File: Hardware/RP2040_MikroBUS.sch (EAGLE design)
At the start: 78 parts, among them J1 SWD, J3 Qwiic, J5 USB C, J6 microSD, J9 MIKROBUS_SMD_BLACK1, Q1 20V/4.2A/52mΩ/1.4W, U2 MAX17048, U3 MCP73831, U4 W25QXX128MBIT, U5 RP2040, U7 3.3V, Y2 12MHz

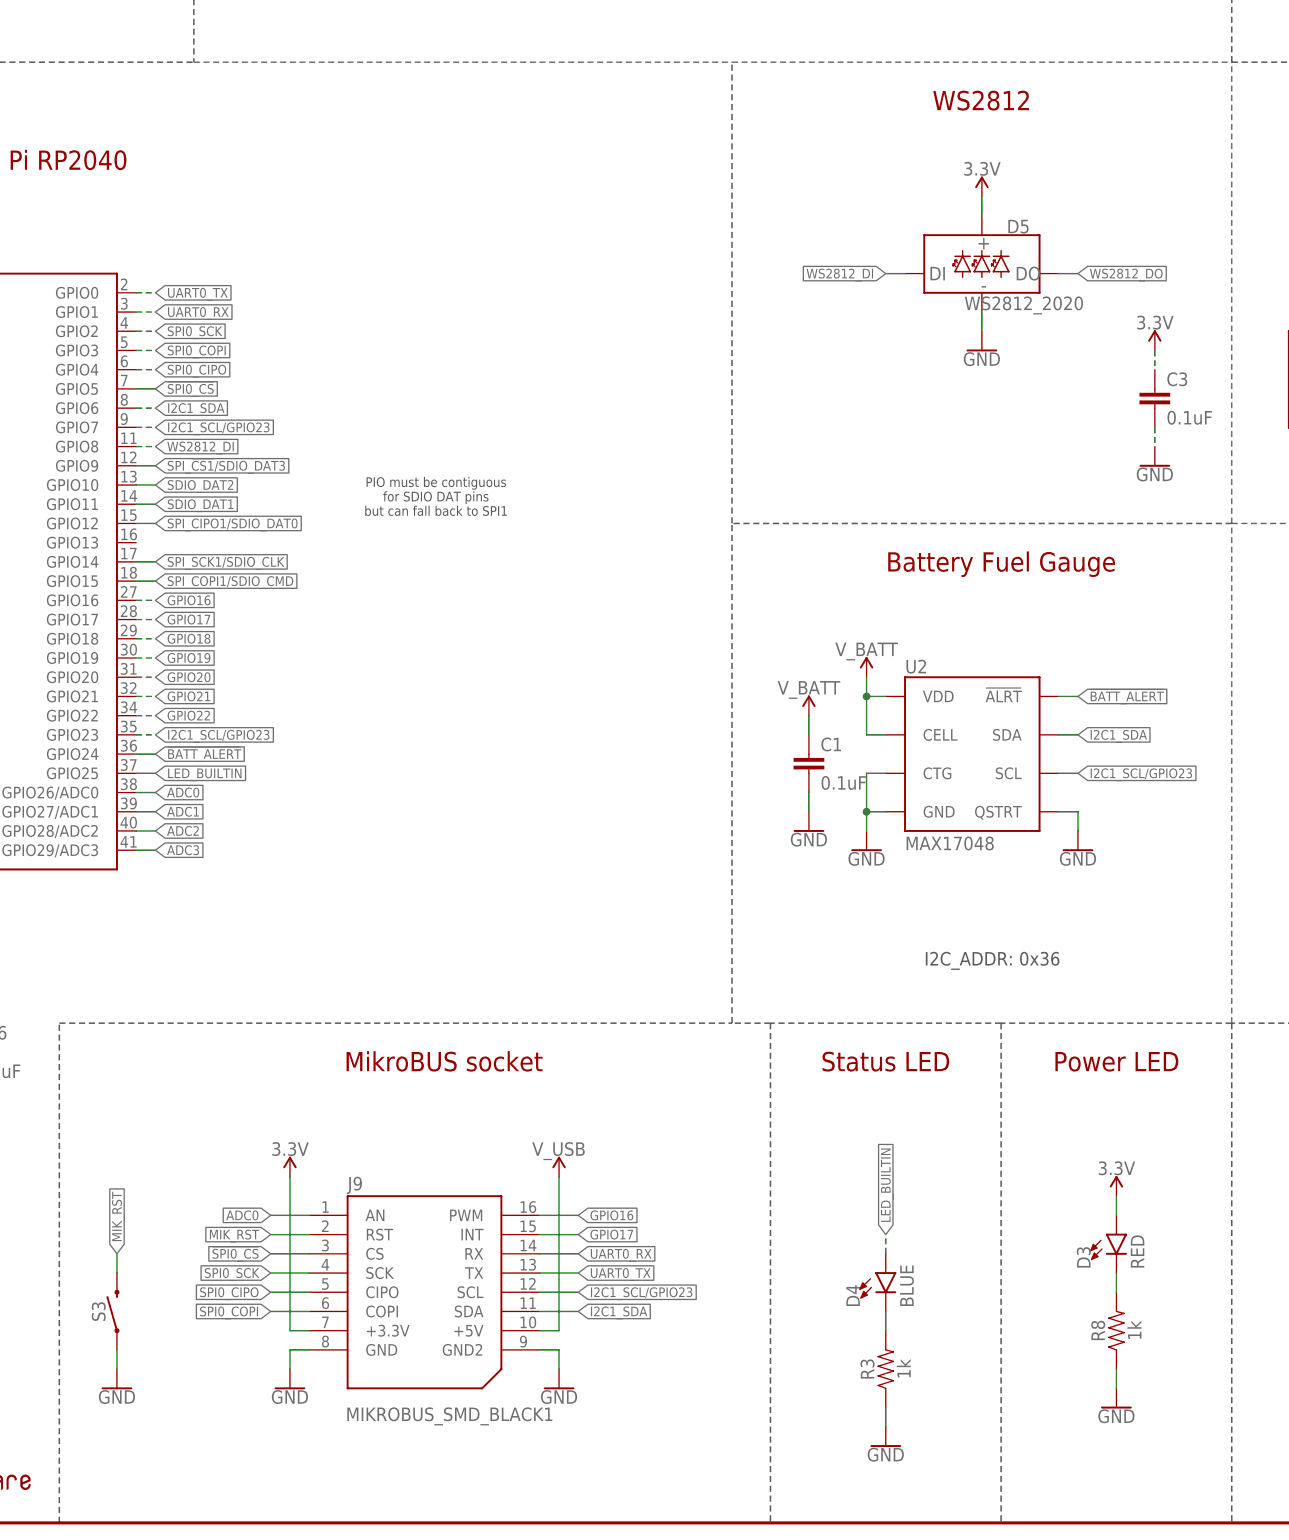
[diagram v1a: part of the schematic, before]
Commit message: Design review before ordering changes
* Add a pullup and NC jumper on the CS line
* A jumper on the PWR LED
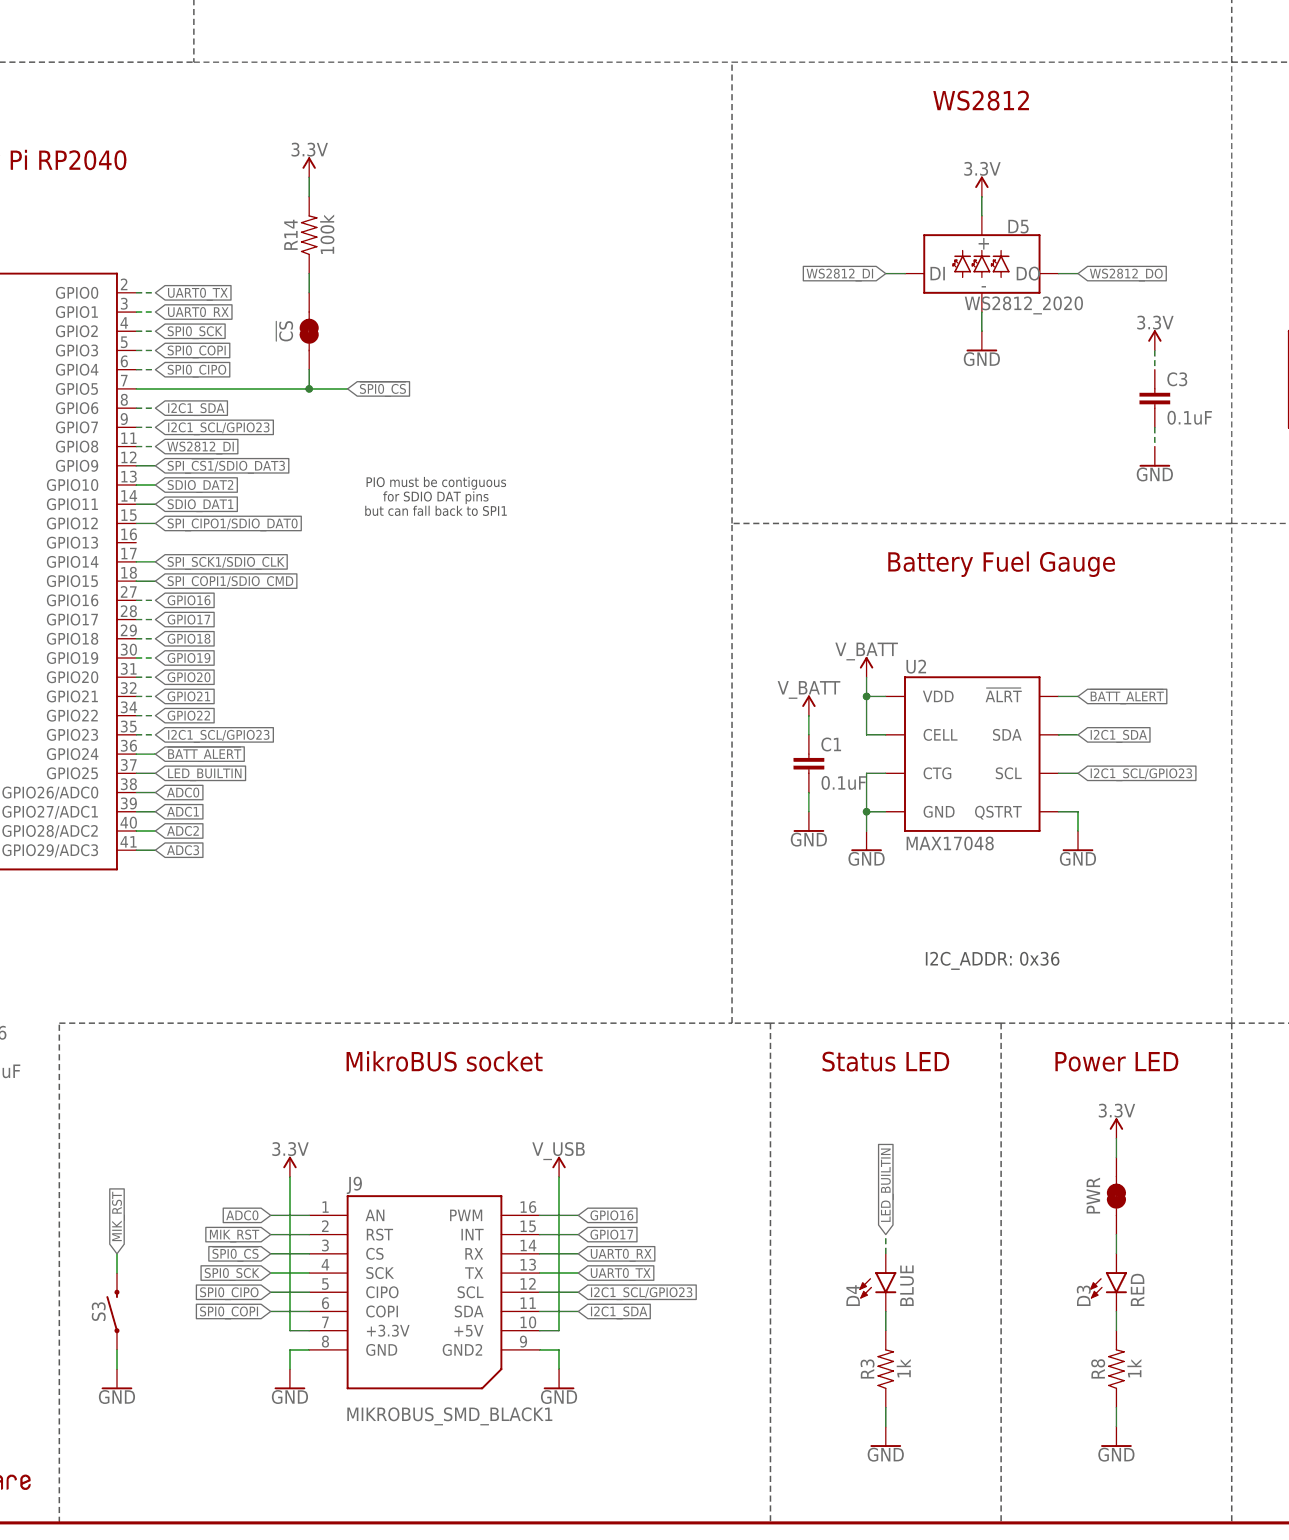
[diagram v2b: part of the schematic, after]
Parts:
- added !CS!, PWR: JUMPER-SMT_2_NC_TRACE_SILK, SparkFun-Jumpers:JUMPER-SMT_2_NC_TRACE_SILK
- added R14: 100k, SparkFun-Resistors:100KOHM-0603-1/10W-1%
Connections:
- new net N$10: D3.A, PWR.1
- new net N$8: !CS!.2, R14.1
- net !SPI0_CS!: now also !CS!.1
- net 3.3V: now also PWR.2, R14.2; no longer D3.A
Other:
- moved on the sheet: D3, R8
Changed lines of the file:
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@@
 <?xml version="1.0" encoding="utf-8"?>
 <!DOCTYPE eagle SYSTEM "eagle.dtd">
-<eagle version="9.4.2">
+<eagle version="9.5.2">
 <drawing>
 <settings>
-<setting alwaysvectorfont="yes"/>
+<setting alwaysvectorfont="no"/>
 <setting keepoldvectorfont="yes"/>
 <setting verticaltext="up"/>
@@
 <part name="SUPPLY39" library="SparkFun-PowerSymbols" deviceset="3.3V" device=""/>
 <part name="GND46" library="SparkFun-PowerSymbols" deviceset="GND" device=""/>
+<part name="!CS!" library="SparkFun-Jumpers" deviceset="JUMPER-SMT_2_NC_TRACE" device="_SILK" package3d_urn="urn:adsk.eagle:package:39281/1"/>
+<part name="R14" library="SparkFun-Resistors" deviceset="100KOHM" device="-0603-1/10W-1%" value="100k"/>
+<part name="SUPPLY13" library="SparkFun-PowerSymbols" deviceset="3.3V" device=""/>
+<part name="PWR" library="SparkFun-Jumpers" deviceset="JUMPER-SMT_2_NC_TRACE" device="_SILK" package3d_urn="urn:adsk.eagle:package:39281/1"/>
 </parts>
 <sheets>
@@
 <attribute name="VALUE" x="199.644" y="233.68" size="1.778" layer="96" font="vector" rot="R90" align="top-center"/>
 </instance>
-<instance part="R8" gate="G$1" x="243.84" y="25.4" smashed="yes" rot="R90">
-<attribute name="NAME" x="242.316" y="25.4" size="1.778" layer="95" font="vector" rot="R90" align="bottom-center"/>
-<attribute name="VALUE" x="245.364" y="25.4" size="1.778" layer="96" font="vector" rot="R90" align="top-center"/>
-</instance>
-<instance part="D3" gate="G$1" x="243.84" y="38.1" smashed="yes">
-<attribute name="NAME" x="240.411" y="33.528" size="1.778" layer="95" font="vector" rot="R90"/>
-<attribute name="VALUE" x="245.745" y="33.528" size="1.778" layer="96" font="vector" rot="R90" align="top-left"/>
-</instance>
-<instance part="GND41" gate="1" x="243.84" y="15.24" smashed="yes">
-<attribute name="VALUE" x="243.84" y="14.986" size="1.778" layer="96" align="top-center"/>
-</instance>
-<instance part="SUPPLY36" gate="G$1" x="243.84" y="43.18" smashed="yes">
-<attribute name="VALUE" x="243.84" y="45.974" size="1.778" layer="96" align="bottom-center"/>
+<instance part="R8" gate="G$1" x="243.84" y="20.32" smashed="yes" rot="R90">
+<attribute name="NAME" x="242.316" y="20.32" size="1.778" layer="95" font="vector" rot="R90" align="bottom-center"/>
+<attribute name="VALUE" x="245.364" y="20.32" size="1.778" layer="96" font="vector" rot="R90" align="top-center"/>
+</instance>
+<instance part="D3" gate="G$1" x="243.84" y="33.02" smashed="yes">
+<attribute name="NAME" x="240.411" y="28.448" size="1.778" layer="95" font="vector" rot="R90"/>
+<attribute name="VALUE" x="245.745" y="28.448" size="1.778" layer="96" font="vector" rot="R90" align="top-left"/>
+</instance>
+<instance part="GND41" gate="1" x="243.84" y="10.16" smashed="yes">
+<attribute name="VALUE" x="243.84" y="9.906" size="1.778" layer="96" align="top-center"/>
+</instance>
+<instance part="SUPPLY36" gate="G$1" x="243.84" y="50.8" smashed="yes">
+<attribute name="VALUE" x="243.84" y="53.594" size="1.778" layer="96" align="bottom-center"/>
 </instance>
 <instance part="GND42" gate="1" x="386.08" y="215.9" smashed="yes">
@@
 <instance part="GND46" gate="1" x="226.06" y="154.94" smashed="yes">
 <attribute name="VALUE" x="226.06" y="154.686" size="1.778" layer="96" align="top-center"/>
+</instance>
+<instance part="!CS!" gate="G$1" x="137.16" y="157.48" smashed="yes" rot="R90">
+<attribute name="NAME" x="134.112" y="157.48" size="1.778" layer="95" font="vector" rot="R90" align="center"/>
+</instance>
+<instance part="R14" gate="G$1" x="137.16" y="170.18" smashed="yes" rot="R90">
+<attribute name="NAME" x="135.636" y="170.18" size="1.778" layer="95" font="vector" rot="R90" align="bottom-center"/>
+<attribute name="VALUE" x="138.684" y="170.18" size="1.778" layer="96" font="vector" rot="R90" align="top-center"/>
+</instance>
+<instance part="SUPPLY13" gate="G$1" x="137.16" y="177.8" smashed="yes">
+<attribute name="VALUE" x="137.16" y="180.594" size="1.778" layer="96" align="bottom-center"/>
+</instance>
+<instance part="PWR" gate="G$1" x="243.84" y="43.18" smashed="yes" rot="R90">
+<attribute name="NAME" x="240.792" y="43.18" size="1.778" layer="95" font="vector" rot="R90" align="center"/>
 </instance>
 </instances>
@@
 </segment>
 <segment>
-<pinref part="D3" gate="G$1" pin="A"/>
-<wire x1="243.84" y1="40.64" x2="243.84" y2="43.18" width="0.1524" layer="91"/>
-<pinref part="SUPPLY36" gate="G$1" pin="3.3V"/>
-</segment>
-<segment>
 <pinref part="J9" gate="J1" pin="+3.3V"/>
 <wire x1="137.16" y1="25.4" x2="134.62" y2="25.4" width="0.1524" layer="91"/>
@@
 <wire x1="226.06" y1="172.72" x2="226.06" y2="175.26" width="0.1524" layer="91"/>
 <pinref part="SUPPLY39" gate="G$1" pin="3.3V"/>
+</segment>
+<segment>
+<pinref part="R14" gate="G$1" pin="2"/>
+<pinref part="SUPPLY13" gate="G$1" pin="3.3V"/>
+<wire x1="137.16" y1="175.26" x2="137.16" y2="177.8" width="0.1524" layer="91"/>
+</segment>
+<segment>
+<pinref part="PWR" gate="G$1" pin="2"/>
+<pinref part="SUPPLY36" gate="G$1" pin="3.3V"/>
+<wire x1="243.84" y1="48.26" x2="243.84" y2="50.8" width="0.1524" layer="91"/>
 </segment>
 </net>
@@
 <segment>
 <pinref part="R8" gate="G$1" pin="1"/>
-<wire x1="243.84" y1="20.32" x2="243.84" y2="17.78" width="0.1524" layer="91"/>
+<wire x1="243.84" y1="15.24" x2="243.84" y2="12.7" width="0.1524" layer="91"/>
 <pinref part="GND41" gate="1" pin="GND"/>
 </segment>
@@
 <pinref part="D3" gate="G$1" pin="C"/>
 <pinref part="R8" gate="G$1" pin="2"/>
-<wire x1="243.84" y1="33.02" x2="243.84" y2="30.48" width="0.1524" layer="91"/>
+<wire x1="243.84" y1="27.94" x2="243.84" y2="25.4" width="0.1524" layer="91"/>
 </segment>
 </net>
@@
 <segment>
 <pinref part="U5" gate="U1" pin="GPIO5"/>
-<wire x1="114.3" y1="149.86" x2="116.84" y2="149.86" width="0.1524" layer="91"/>
-<label x="116.84" y="149.86" size="1.27" layer="95" xref="yes"/>
+<wire x1="114.3" y1="149.86" x2="137.16" y2="149.86" width="0.1524" layer="91"/>
+<label x="142.24" y="149.86" size="1.27" layer="95" xref="yes"/>
+<pinref part="!CS!" gate="G$1" pin="1"/>
+<wire x1="137.16" y1="149.86" x2="142.24" y2="149.86" width="0.1524" layer="91"/>
+<wire x1="137.16" y1="152.4" x2="137.16" y2="149.86" width="0.1524" layer="91"/>
+<junction x="137.16" y="149.86"/>
 </segment>
 <segment>
@@
 </segment>
 </net>
+<net name="N$8" class="0">
+<segment>
+<pinref part="!CS!" gate="G$1" pin="2"/>
+<pinref part="R14" gate="G$1" pin="1"/>
+<wire x1="137.16" y1="162.56" x2="137.16" y2="165.1" width="0.1524" layer="91"/>
+</segment>
+</net>
+<net name="N$10" class="0">
+<segment>
+<pinref part="D3" gate="G$1" pin="A"/>
+<pinref part="PWR" gate="G$1" pin="1"/>
+<wire x1="243.84" y1="35.56" x2="243.84" y2="38.1" width="0.1524" layer="91"/>
+</segment>
+</net>

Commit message: Update labels
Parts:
- removed !CS!: JUMPER-SMT_2_NC_TRACE_SILK, SparkFun-Jumpers:JUMPER-SMT_2_NC_TRACE_SILK
- removed R14: 100k, SparkFun-Resistors:100KOHM-0603-1/10W-1%
- removed S3: MOMENTARY-SWITCH-SPST-SMD-5.2MM-TALL, SparkFun-Switches:MOMENTARY-SWITCH-SPST-SMD-5.2MM-TALL
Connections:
- removed net N$8: !CS!.2, R14.1
- net !SPI0_CS!: no longer !CS!.1
- net 3.3V: no longer R14.2
- net GND: no longer S3.1
- net MIK_RST: no longer S3.2
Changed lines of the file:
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@@
 <part name="SUPPLY37" library="SparkFun-PowerSymbols" deviceset="3.3V" device=""/>
 <part name="SUPPLY38" library="SparkFun-PowerSymbols" deviceset="V_USB" device=""/>
-<part name="S3" library="SparkFun-Switches" deviceset="MOMENTARY-SWITCH-SPST" device="-SMD-5.2MM-TALL"/>
-<part name="GND45" library="SparkFun-PowerSymbols" deviceset="GND" device=""/>
 <part name="U$17" library="SparkFun-Aesthetics" deviceset="RASPI_RP2040_LOGO" device="_10MM"/>
 <part name="U$73" library="SparkFun-Aesthetics" deviceset="RASPI_RP2040_LOGO" device="_10MM"/>
@@
 <part name="SUPPLY39" library="SparkFun-PowerSymbols" deviceset="3.3V" device=""/>
 <part name="GND46" library="SparkFun-PowerSymbols" deviceset="GND" device=""/>
-<part name="!CS!" library="SparkFun-Jumpers" deviceset="JUMPER-SMT_2_NC_TRACE" device="_SILK" package3d_urn="urn:adsk.eagle:package:39281/1"/>
-<part name="R14" library="SparkFun-Resistors" deviceset="100KOHM" device="-0603-1/10W-1%" value="100k"/>
-<part name="SUPPLY13" library="SparkFun-PowerSymbols" deviceset="3.3V" device=""/>
 <part name="PWR" library="SparkFun-Jumpers" deviceset="JUMPER-SMT_2_NC_TRACE" device="_SILK" package3d_urn="urn:adsk.eagle:package:39281/1"/>
 </parts>
@@
 <attribute name="VALUE" x="170.18" y="48.514" size="1.778" layer="96" align="bottom-center"/>
 </instance>
-<instance part="S3" gate="G$1" x="111.76" y="27.94" smashed="yes" rot="R90">
-<attribute name="NAME" x="110.236" y="27.94" size="1.778" layer="95" font="vector" rot="R90" align="bottom-center"/>
-</instance>
-<instance part="GND45" gate="1" x="111.76" y="17.78" smashed="yes">
-<attribute name="VALUE" x="111.76" y="17.526" size="1.778" layer="96" align="top-center"/>
-</instance>
 <instance part="U$17" gate="G$1" x="30.48" y="12.7" smashed="yes"/>
 <instance part="U$73" gate="G$1" x="30.48" y="12.7" smashed="yes"/>
@@
 <instance part="GND46" gate="1" x="226.06" y="154.94" smashed="yes">
 <attribute name="VALUE" x="226.06" y="154.686" size="1.778" layer="96" align="top-center"/>
-</instance>
-<instance part="!CS!" gate="G$1" x="137.16" y="157.48" smashed="yes" rot="R90">
-<attribute name="NAME" x="134.112" y="157.48" size="1.778" layer="95" font="vector" rot="R90" align="center"/>
-</instance>
-<instance part="R14" gate="G$1" x="137.16" y="170.18" smashed="yes" rot="R90">
-<attribute name="NAME" x="135.636" y="170.18" size="1.778" layer="95" font="vector" rot="R90" align="bottom-center"/>
-<attribute name="VALUE" x="138.684" y="170.18" size="1.778" layer="96" font="vector" rot="R90" align="top-center"/>
-</instance>
-<instance part="SUPPLY13" gate="G$1" x="137.16" y="177.8" smashed="yes">
-<attribute name="VALUE" x="137.16" y="180.594" size="1.778" layer="96" align="bottom-center"/>
 </instance>
 <instance part="PWR" gate="G$1" x="243.84" y="43.18" smashed="yes" rot="R90">
@@
 </segment>
 <segment>
-<pinref part="R14" gate="G$1" pin="2"/>
-<pinref part="SUPPLY13" gate="G$1" pin="3.3V"/>
-<wire x1="137.16" y1="175.26" x2="137.16" y2="177.8" width="0.1524" layer="91"/>
-</segment>
-<segment>
 <pinref part="PWR" gate="G$1" pin="2"/>
 <pinref part="SUPPLY36" gate="G$1" pin="3.3V"/>
@@
 <wire x1="170.18" y1="22.86" x2="170.18" y2="20.32" width="0.1524" layer="91"/>
 <pinref part="GND44" gate="1" pin="GND"/>
-</segment>
-<segment>
-<wire x1="111.76" y1="22.86" x2="111.76" y2="20.32" width="0.1524" layer="91"/>
-<pinref part="S3" gate="G$1" pin="1"/>
-<pinref part="GND45" gate="1" pin="GND"/>
 </segment>
 <segment>
@@
 <label x="132.08" y="38.1" size="1.27" layer="95" rot="R180" xref="yes"/>
 </segment>
-<segment>
-<wire x1="111.76" y1="33.02" x2="111.76" y2="35.56" width="0.1524" layer="91"/>
-<label x="111.76" y="35.56" size="1.27" layer="95" font="vector" rot="R90" xref="yes"/>
-<pinref part="S3" gate="G$1" pin="2"/>
-</segment>
 </net>
 <net name="!SPI0_CS!" class="0">
 <segment>
 <pinref part="U5" gate="U1" pin="GPIO5"/>
-<wire x1="114.3" y1="149.86" x2="137.16" y2="149.86" width="0.1524" layer="91"/>
-<label x="142.24" y="149.86" size="1.27" layer="95" xref="yes"/>
-<pinref part="!CS!" gate="G$1" pin="1"/>
-<wire x1="137.16" y1="149.86" x2="142.24" y2="149.86" width="0.1524" layer="91"/>
-<wire x1="137.16" y1="152.4" x2="137.16" y2="149.86" width="0.1524" layer="91"/>
-<junction x="137.16" y="149.86"/>
+<wire x1="114.3" y1="149.86" x2="116.84" y2="149.86" width="0.1524" layer="91"/>
+<label x="116.84" y="149.86" size="1.27" layer="95" xref="yes"/>
 </segment>
 <segment>
@@
 </segment>
 </net>
-<net name="N$8" class="0">
-<segment>
-<pinref part="!CS!" gate="G$1" pin="2"/>
-<pinref part="R14" gate="G$1" pin="1"/>
-<wire x1="137.16" y1="162.56" x2="137.16" y2="165.1" width="0.1524" layer="91"/>
-</segment>
-</net>
